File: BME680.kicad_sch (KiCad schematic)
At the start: 23 parts, among them IC1 BME680, Q2 BSS138, U2 AP2112K-3.3

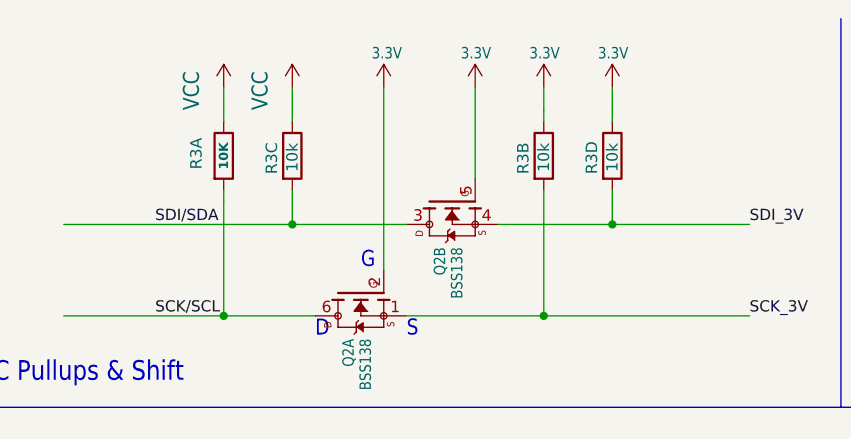
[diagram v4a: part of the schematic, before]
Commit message: fixed mistake on resistors
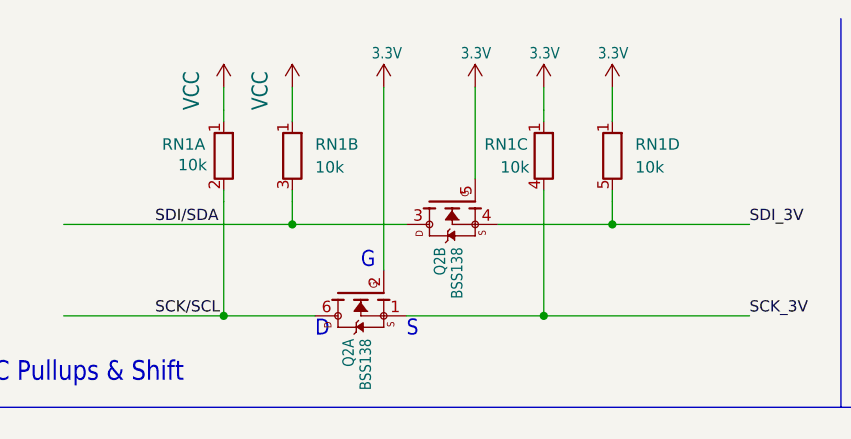
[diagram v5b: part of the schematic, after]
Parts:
- removed R3A: 10K, BME680:RESPACK_4X0603, symbol Device:R
- removed R3B, R3C, R3D: 10k, symbol Device:R
- added RN1: 10k, Resistor_THT:R_Array_SIP5, symbol Device:R_Network04_Split
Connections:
- net 3.3V: now also RN1.1 (R1), RN1.1 (R1)
- net SCK/SCL: now also RN1.2 (R1.2)
- net SCK_3V: now also RN1.4 (R3.2)
- net SDI/SDA: now also RN1.3 (R2.2)
- net SDI_3V: now also RN1.5 (R4.2)
- net VCC: now also RN1.1 (R1), RN1.1 (R1)

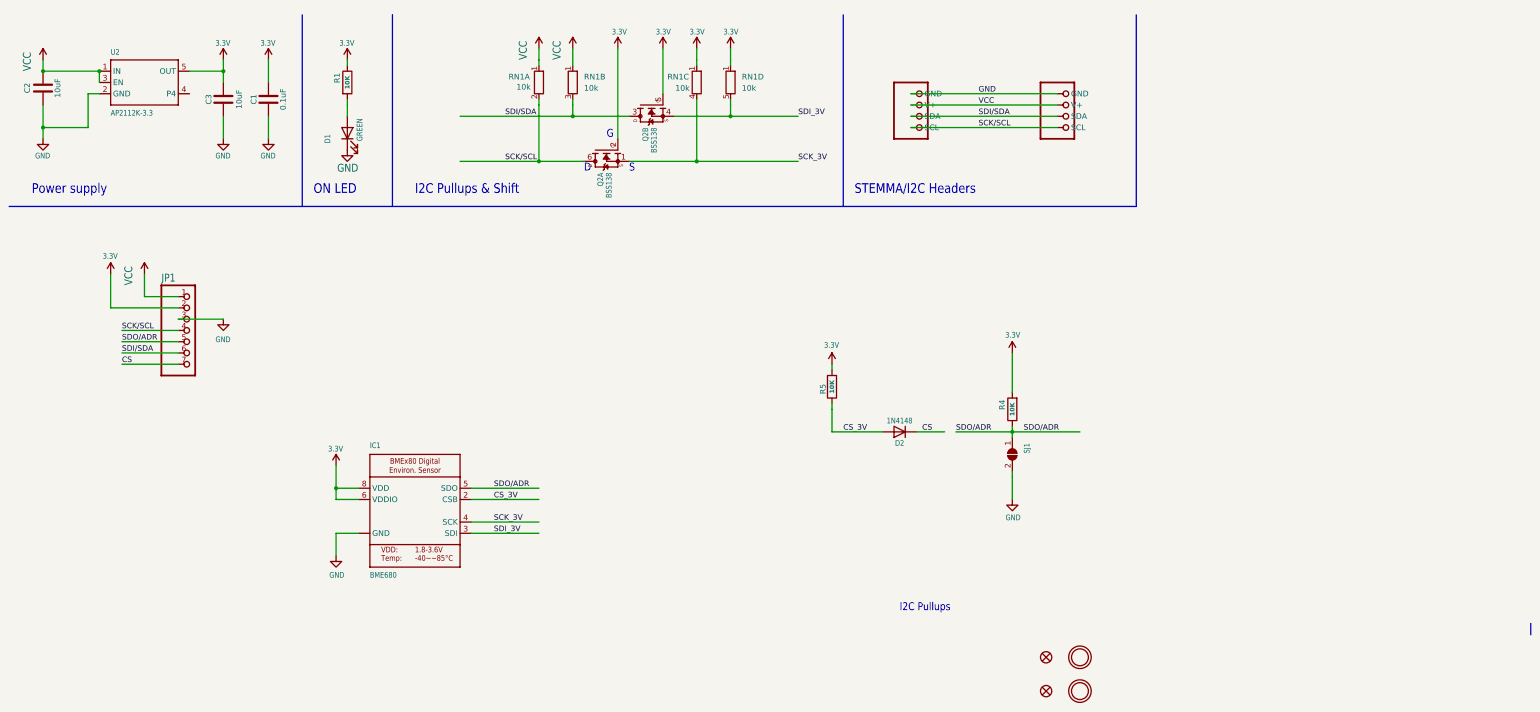
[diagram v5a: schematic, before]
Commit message: updated nmos libraty
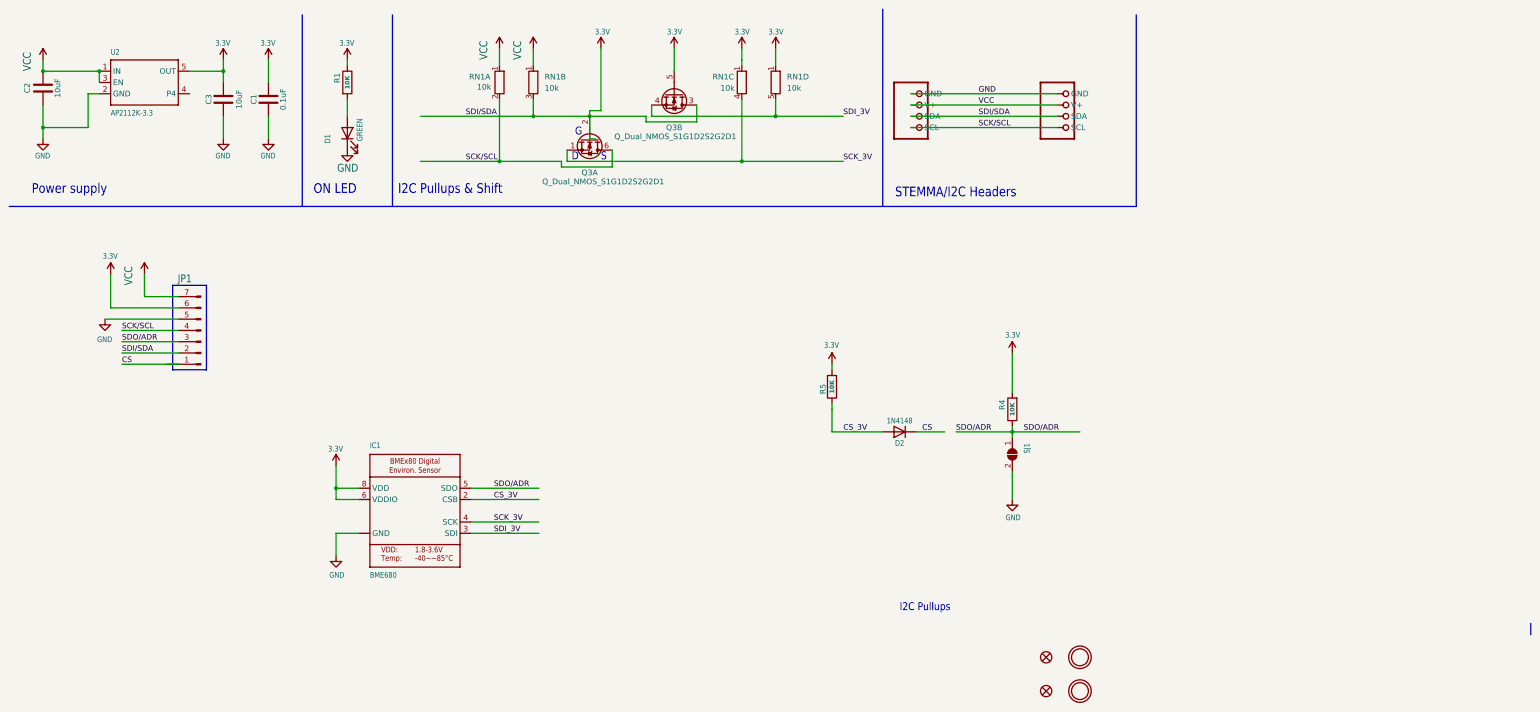
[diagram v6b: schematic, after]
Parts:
- removed Q2: BSS138, BME680:SOT363, symbol BME680-eagle-import:MOSFET-N_DUAL
- added Q3: Q_Dual_NMOS_S1G1D2S2G2D1, symbol Device:Q_Dual_NMOS_S1G1D2S2G2D1
- JP1: symbol BME680-eagle-import:HEADER-1X770MIL -> Connector:Conn_01x07_Pin
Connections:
- net SDI/SDA is gone; now on net 3.3V: CONN3.3 (SDA), CONN4.3 (SDA), JP1.6 (Pin_6), RN1.3 (R2.2)
- net 3.3V: now also Q3.2 (G), Q3.3 (D), Q3.5 (G)
- net CS: now also JP1.1 (Pin_1); no longer JP1.7
- net GND: now also JP1.5 (Pin_5); no longer JP1.3
- net SCK/SCL: now also Q3.6 (D)
- net SCK_3V: now also Q3.1 (S)
- net SDI_3V: now also Q3.4 (S)
- net SDO/ADR: now also JP1.3 (Pin_3); no longer JP1.5
- net VCC: now also JP1.7 (Pin_7); no longer JP1.1
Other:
- moved on the sheet: RN1A, RN1B, RN1C, RN1D
